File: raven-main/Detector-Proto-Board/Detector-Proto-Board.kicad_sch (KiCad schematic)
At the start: 17 parts, among them IC1 ADA4817-1ARDZ-R7, J1 Conn_01x04, U9 TLV3201AIDCKT

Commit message: feat:PCB layout changes - example
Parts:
- added H101, H102, H103, H104: MountingHole_Pad, MountingHole:MountingHole_3.2mm_M3_DIN965_Pad, symbol Mechanical:MountingHole_Pad
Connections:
- net +5V: now also J1.4 (Pin_4); no longer J1.2 (Pin_2)
- net Detector_Out_A: now also J1.2 (Pin_2); no longer J1.4 (Pin_4)
- net GND: now also H101.1, H102.1, H103.1, H104.1
- net OUT: now reaches C35.2, IC1.6 (OUT), R27.2, U9.4 (IN-)
- net OUT: now also IC1.1 (FB)
- no-connect marks 2 -> 1

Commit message: Add 2.5V pedestal bias to fix TIA operating point on single supply
Fix amplifier DC operating point with 2.5V pedestal bias

The ADA4817 TIA output rested at 0V with +IN grounded, but on a single
0-5V supply the output cannot swing below ~1.4V, pinning the amplifier
against the rail. Bias +IN to a 2.5V pedestal so the output rests
mid-range and photocurrent pulses swing into its linear region.

- Add pedestal divider: R33/R34 (10k) + C40 (1uF) generating Vped (2.5V)
- Reroute IC1 +IN from GND to Vped
- Re-reference threshold divider to Vped: R28 to GND, R32 to Vped
- R31 200K->300K, R32 200->300 to keep the 5-25mV hysteresis band
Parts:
- added C40: 1uF, Capacitor_SMD:C_0402_1005Metric, symbol Device:C
- added R33, R34: 10k, Resistor_SMD:R_0402_1005Metric, symbol Device:R
- R31: value 200K -> 300K
- R32: value 200 -> 300
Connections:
- net +5V: now also R33.1; no longer R28.2
- net GND: now also R28.2, C40.2, R34.2; no longer IC1.3 (+IN), R32.1
- new net Vped: C40.1, IC1.3 (+IN), R32.1, R33.2, R34.1

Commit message: Added essential changes to circuit schematic
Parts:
- added C1: 330p, Capacitor_SMD:C_0402_1005Metric, symbol Device:C
- added C41: 0.5pF, Capacitor_SMD:C_0402_1005Metric, symbol Device:C
- added R35: 1.6k, Resistor_SMD:R_0402_1005Metric, symbol Device:R
- R29: footprint Resistor_SMD:R_0402_1005Metric -> Potentiometer_THT:Potentiometer_Runtron_RM-063_Horizontal
- R31: value 300K -> 390K
- R32: value 300 -> 33
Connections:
- net GND: now also C1.2
- net OUT: now also C41.2, R35.1; no longer U9.4 (IN-)
- net at C35.1, D4.2 (A), IC1.2 (-IN)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: now also C41.1
- new net: C1.1, R35.2, U9.4 (IN-)

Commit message: Added some initial pcb changes from Revision 2
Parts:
- removed D1: SMAJ58A, Diode_SMD:D_SMA, symbol SMAJ58A:SMAJ58A
- added D1: SMAJ26A, Diode_SMD:D_SMA, symbol Diode:SMAJ26A
- added J2: Conn_01x01, symbol Connector_Generic:Conn_01x01
- added J3: Conn_01x02, symbol Connector_Generic:Conn_01x02
- added R1: 0, symbol Device:R
- added R36: 1G, Resistor_SMD:R_0402_1005Metric, symbol Device:R
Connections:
- net +50V: now also D1.1 (A1)
- net GND: now also D1.2 (A2)
- net OUT: now also R36.2
- net V_thresh_A: now also J2.1 (Pin_1), R1.2; no longer R28.1, R29.1
- net at C35.1, C41.1, D4.2 (A)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: now also J3.2 (Pin_2), R36.1
- net at C39.1, D4.1 (K), R30.2: now also J3.1 (Pin_1)
- new net: R1.1, R28.1, R29.1

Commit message: Updated pcb schematic for proto board
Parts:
- added D5: BPW34, OptoDevice:Osram_DIL2_4.3x4.65mm_P5.08mm, symbol Sensor_Optical:BPW34
- added R38: 0, Resistor_SMD:R_0402_1005Metric, symbol Device:R
- added TP1: OUT, TestPoint:TestPoint_Pad_D2.5mm, symbol Connector:TestPoint
- added TP2: V_thresh, TestPoint:TestPoint_Pad_D2.5mm, symbol Connector:TestPoint
- added TP3: Vped, TestPoint:TestPoint_Pad_D2.5mm, symbol Connector:TestPoint
- added TP4: Detector_Out, TestPoint:TestPoint_Pad_D2.5mm, symbol Connector:TestPoint
- added TP5: GND, TestPoint:TestPoint_Pad_D2.5mm, symbol Connector:TestPoint
- J2: footprint (none) -> Connector_PinHeader_2.54mm:PinHeader_1x01_P2.54mm_Vertical
- J3: footprint (none) -> Connector_PinHeader_2.54mm:PinHeader_1x02_P2.54mm_Vertical
- R1: footprint (none) -> Resistor_SMD:R_0402_1005Metric
- R29: footprint Potentiometer_THT:Potentiometer_Runtron_RM-063_Horizontal -> 3224X:SOT_502E
- renumbered C41 to C42, R36 to R37
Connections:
- net Detector_Out_A: now also TP4.1
- net GND: now also TP5.1
- net OUT: now also TP1.1
- net V_thresh_A: now also TP2.1
- net Vped: now also R38.2, TP3.1; no longer R33.2
- net at C35.1, C42.1, D4.2 (A)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: now also D5.2 (A)
- net at C39.1, D4.1 (K), J3.1 (Pin_1)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: now also D5.1 (K)
- net +50V renamed +25V
- new net: R33.2, R38.1
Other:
- moved on the sheet: R33

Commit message: Repositioned TVS diode
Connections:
- net +25V: no longer J1.1 (Pin_1)
- net GND: no longer D1.2 (A2)
- new net: D1.2 (A2), J1.1 (Pin_1)
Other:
- moved on the sheet: TP5
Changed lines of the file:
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@@
 	)
 	(junction
-		(at 193.04 24.13)
-		(diameter 0)
-		(color 0 0 0 0)
-	)
-	(junction
 		(at 39.37 100.33)
 		(diameter 0)
@@
 	)
 	(junction
-		(at 154.94 104.14)
+		(at 143.51 38.1)
 		(diameter 0)
 		(color 0 0 0 0)
 	)
 	(junction
-		(at 67.31 60.96)
+		(at 154.94 104.14)
 		(diameter 0)
 		(color 0 0 0 0)
 	)
 	(junction
-		(at 67.31 68.58)
+		(at 67.31 60.96)
 		(diameter 0)
 		(color 0 0 0 0)
 	)
 	(junction
-		(at 205.315 24.13)
+		(at 67.31 68.58)
 		(diameter 0)
 		(color 0 0 0 0)
@@
 	(wire
 		(pts
-			(xy 139.7 38.1) (xy 193.04 38.1)
+			(xy 139.7 38.1) (xy 143.51 38.1)
 		)
 		(stroke
@@
 	(wire
 		(pts
-			(xy 168.91 90.17) (xy 168.91 99.06)
+			(xy 193.04 27.94) (xy 201.93 27.94)
 		)
 		(stroke
@@
 	(wire
 		(pts
-			(xy 54.61 35.56) (xy 57.15 35.56)
+			(xy 168.91 90.17) (xy 168.91 99.06)
 		)
 		(stroke
@@
 	(wire
 		(pts
-			(xy 34.29 91.44) (xy 34.29 92.71)
+			(xy 54.61 35.56) (xy 57.15 35.56)
 		)
 		(stroke
@@
 	(wire
 		(pts
-			(xy 123.19 68.58) (xy 135.89 68.58)
+			(xy 34.29 91.44) (xy 34.29 92.71)
 		)
 		(stroke
@@
 	(wire
 		(pts
-			(xy 104.14 66.04) (xy 104.14 60.96)
+			(xy 123.19 68.58) (xy 135.89 68.58)
 		)
 		(stroke
@@
 	(wire
 		(pts
-			(xy 135.89 68.58) (xy 135.89 71.12)
+			(xy 104.14 66.04) (xy 104.14 60.96)
 		)
 		(stroke
@@
 	(wire
 		(pts
-			(xy 165.1 35.56) (xy 168.91 35.56)
+			(xy 135.89 68.58) (xy 135.89 71.12)
 		)
 		(stroke
@@
 	(wire
 		(pts
-			(xy 184.15 24.13) (xy 193.04 24.13)
+			(xy 165.1 35.56) (xy 168.91 35.56)
 		)
 		(stroke
@@
 	(wire
 		(pts
-			(xy 205.315 24.13) (xy 209.55 24.13)
+			(xy 116.84 128.27) (xy 116.84 132.08)
 		)
 		(stroke
@@
 	(wire
 		(pts
-			(xy 116.84 128.27) (xy 116.84 132.08)
+			(xy 200.66 24.13) (xy 201.93 24.13)
 		)
 		(stroke
@@
 	(wire
 		(pts
-			(xy 200.66 24.13) (xy 205.315 24.13)
+			(xy 193.04 33.02) (xy 193.04 27.94)
 		)
 		(stroke
@@
 	(wire
 		(pts
+			(xy 143.51 38.1) (xy 193.04 38.1)
+		)
+		(stroke
+			(width 0)
+			(type default)
+		)
+	)
+	(wire
+		(pts
 			(xy 219.71 86.36) (xy 219.71 96.52)
 		)
@@
 	(wire
 		(pts
-			(xy 193.04 24.13) (xy 193.04 33.02)
+			(xy 39.37 91.44) (xy 39.37 92.71)
 		)
 		(stroke
@@
 	(wire
 		(pts
-			(xy 39.37 91.44) (xy 39.37 92.71)
+			(xy 184.15 40.64) (xy 193.04 40.64)
 		)
 		(stroke
@@
 	(wire
 		(pts
-			(xy 184.15 40.64) (xy 193.04 40.64)
+			(xy 201.93 27.94) (xy 201.93 24.13)
 		)
 		(stroke
@@
 	(wire
 		(pts
+			(xy 184.15 24.13) (xy 193.04 24.13)
+		)
+		(stroke
+			(width 0)
+			(type default)
+		)
+	)
+	(wire
+		(pts
 			(xy 232.41 67.31) (xy 232.41 101.6)
 		)
@@
 	(symbol
 		(lib_id "Connector:TestPoint")
-		(at 205.315 24.13 0)
+		(at 143.51 38.1 0)
 		(unit 1)
 		(body_style 1)
@@
 		(fields_autoplaced yes)
 		(property "Reference" "TP5"
-			(at 207.855 19.5579 0)
+			(at 146.05 33.5279 0)
 			(show_name no)
 			(do_not_autoplace no)
@@
 		)
 		(property "Value" "GND"
-			(at 207.855 22.0979 0)
+			(at 146.05 36.0679 0)
 			(show_name no)
 			(do_not_autoplace no)
@@
 		)
 		(property "Footprint" "TestPoint:TestPoint_Pad_D2.5mm"
-			(at 210.395 24.13 0)
+			(at 148.59 38.1 0)
 			(hide yes)
 			(show_name no)
@@
 		)
 		(property "Datasheet" ""
-			(at 210.395 24.13 0)
+			(at 148.59 38.1 0)
 			(hide yes)
 			(show_name no)
@@
 		)
 		(property "Description" "test point"
-			(at 205.315 24.13 0)
+			(at 143.51 38.1 0)
 			(hide yes)
 			(show_name no)
@@
 					(unit 1)
 				)
-			)
-		)
-	)
-	(symbol
-		(lib_id "power:GND")
-		(at 209.55 24.13 0)
-		(unit 1)
-		(body_style 1)
-		(exclude_from_sim no)
-		(in_bom yes)
-		(on_board yes)
-		(in_pos_files yes)
-		(dnp no)
-		(fields_autoplaced yes)
-		(property "Reference" "#PWR03"
-			(at 209.55 30.48 0)
-			(hide yes)
-			(show_name no)
-			(do_not_autoplace no)
-			(effects
-				(font
-					(size 1.27 1.27)
-				)
-			)
-		)
-		(property "Value" "GND"
-			(at 212.09 25.3999 0)
-			(show_name no)
-			(do_not_autoplace no)
-			(effects
-				(font
-					(size 1.27 1.27)
-				)
-				(justify left)
-			)
-		)
-		(property "Footprint" ""
-			(at 209.55 24.13 0)
-			(hide yes)
-			(show_name no)
-			(do_not_autoplace no)
-			(effects
-				(font
-					(size 1.27 1.27)
-				)
-			)
-		)
-		(property "Datasheet" ""
-			(at 209.55 24.13 0)
-			(hide yes)
-			(show_name no)
-			(do_not_autoplace no)
-			(effects
-				(font
-					(size 1.27 1.27)
-				)
-			)
-		)
-		(property "Description" "Power symbol creates a global label with name \"GND\" , ground"
-			(at 209.55 24.13 0)
-			(hide yes)
-			(show_name no)
-			(do_not_autoplace no)
-			(effects
-				(font
-					(size 1.27 1.27)
-				)
-			)
-		)
-		(pin "1"
-		)
-		(instances
-			(project "Detector-Proto-Board"
-				(path "/8e9b2cb6-291f-43a2-81af-b7790dd07157"
-					(reference "#PWR03")
-					(unit 1)
-				)

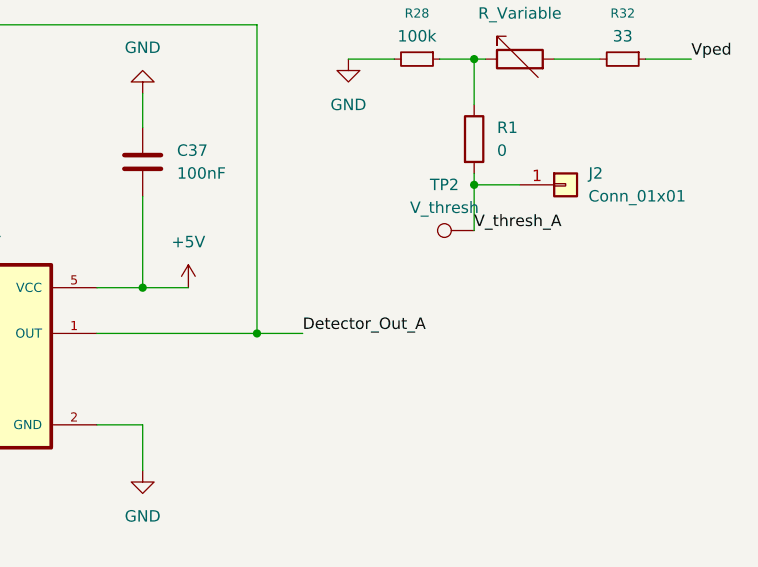
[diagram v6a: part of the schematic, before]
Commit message: Added 3.3V voltage divider to detector board
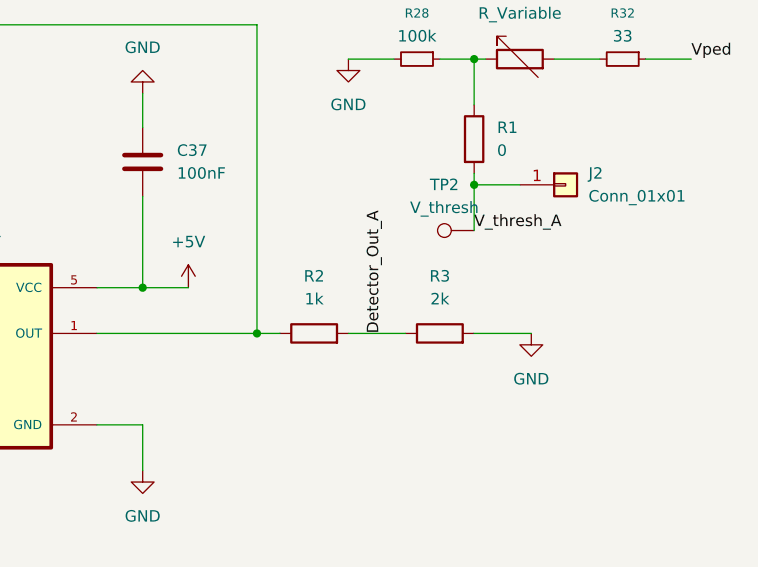
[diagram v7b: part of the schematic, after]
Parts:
- added R2: 1k, Resistor_SMD:R_0402_1005Metric, symbol Device:R
- added R3: 2k, Resistor_SMD:R_0402_1005Metric, symbol Device:R
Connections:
- net Detector_Out_A: now also R2.2, R3.1; no longer R31.2, U9.1 (OUT)
- net GND: now also R3.2
- new net: R2.1, R31.2, U9.1 (OUT)
